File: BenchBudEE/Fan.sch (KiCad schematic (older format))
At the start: 0 parts

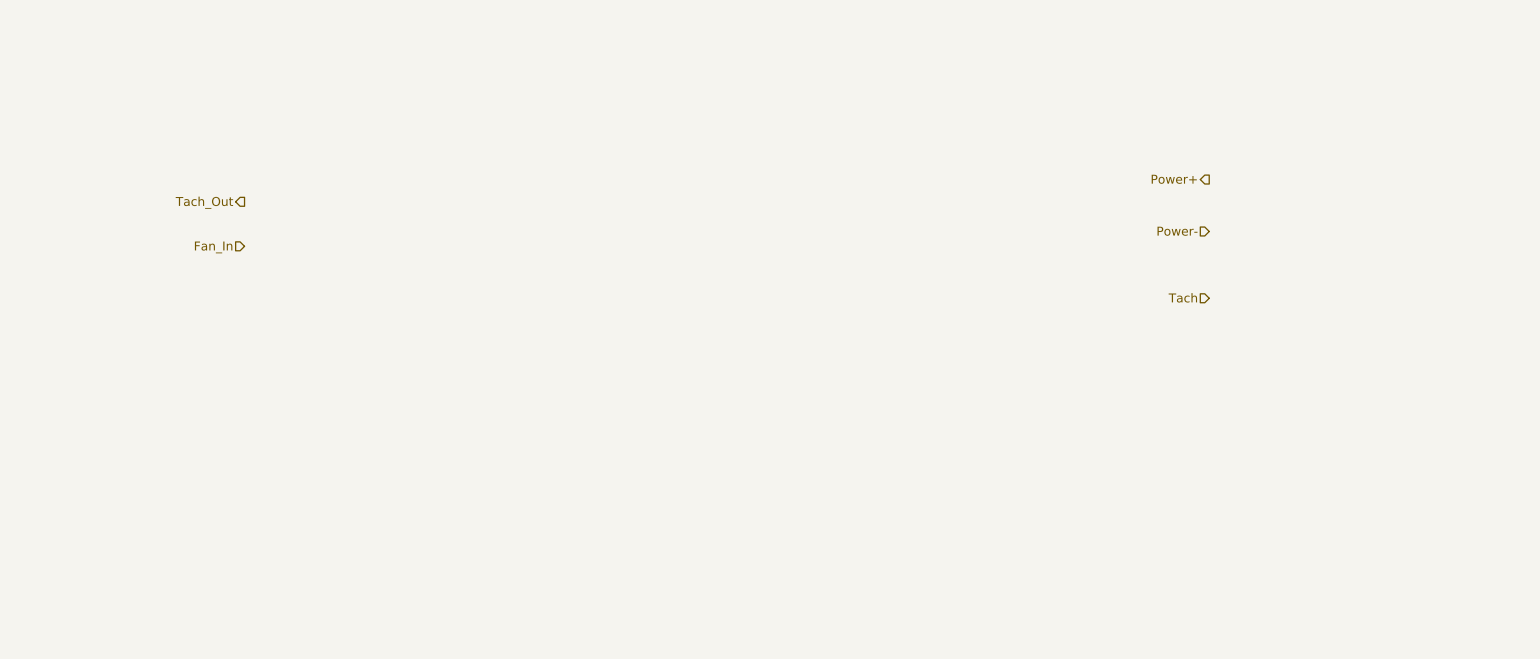
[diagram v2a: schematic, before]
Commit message: Roughly filled in the Fan sheet.
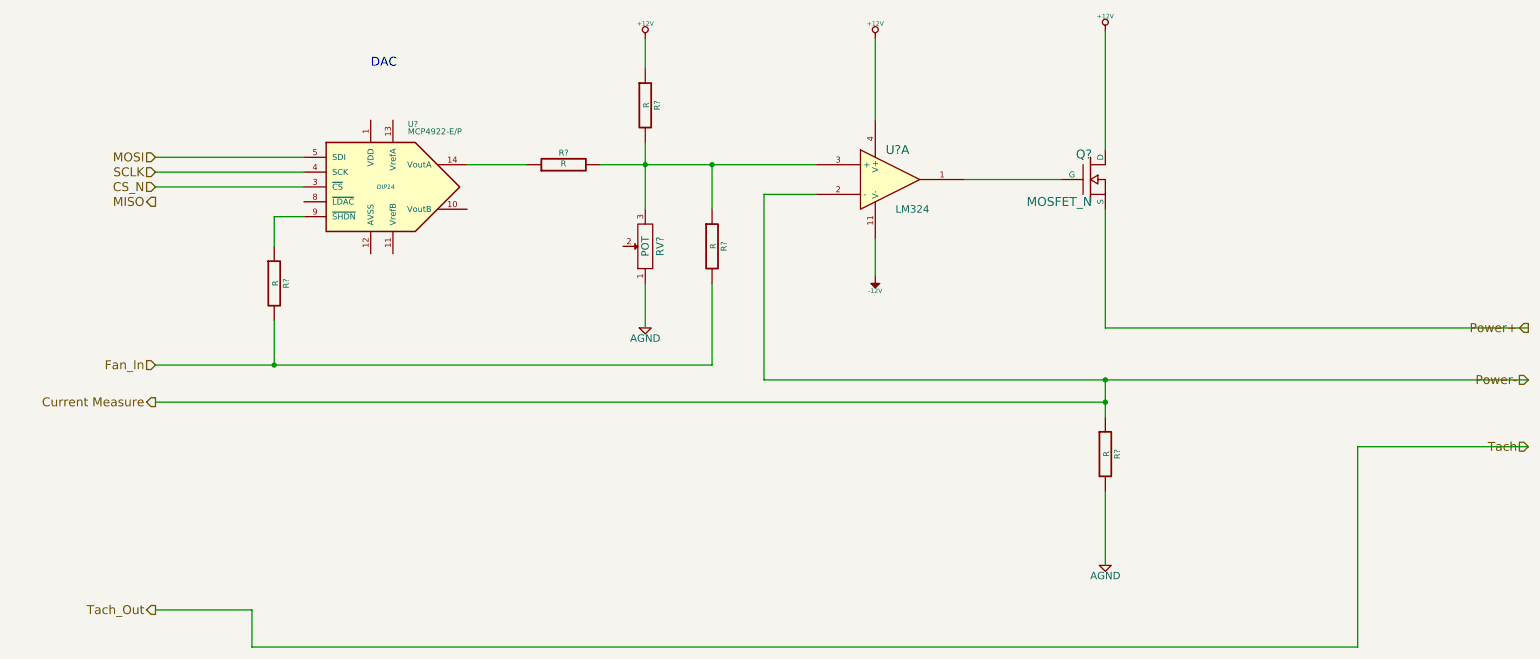
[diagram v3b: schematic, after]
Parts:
- added Q?: MOSFET_N, ~, symbol MOSFET_N
- added R? (x5): R, ~, symbol R
- added RV?: POT, ~, symbol POT
- added U?: LM324, symbol LM324
- added U?: MCP4922-E/P, DIP14, symbol MCP4922-E/P
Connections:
- net Fan_In: now also R?.2, R?.2
- net Power+: now also Q?.S
- new net: Q?.G, U?.1
- new net: R?.1, R?.2, R?.2, RV?.3, U?.3 (+)
- new net: R?.1, U?.14 (VoutA)
- new net: R?.1, U?.9 (~SHDN~)
- new net +12V: Q?.D, R?.1, U?.4 (V+)
- new net -12V: U?.11 (V-)
- new net AGND: R?.2, RV?.1
- new net CS_N: U?.3 (~CS~)
- new net Current Measure: R?.1, U?.2 (-)
- new net MOSI: U?.5 (SDI)
- new net SCLK: U?.4 (SCK)
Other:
- note added: "DAC"

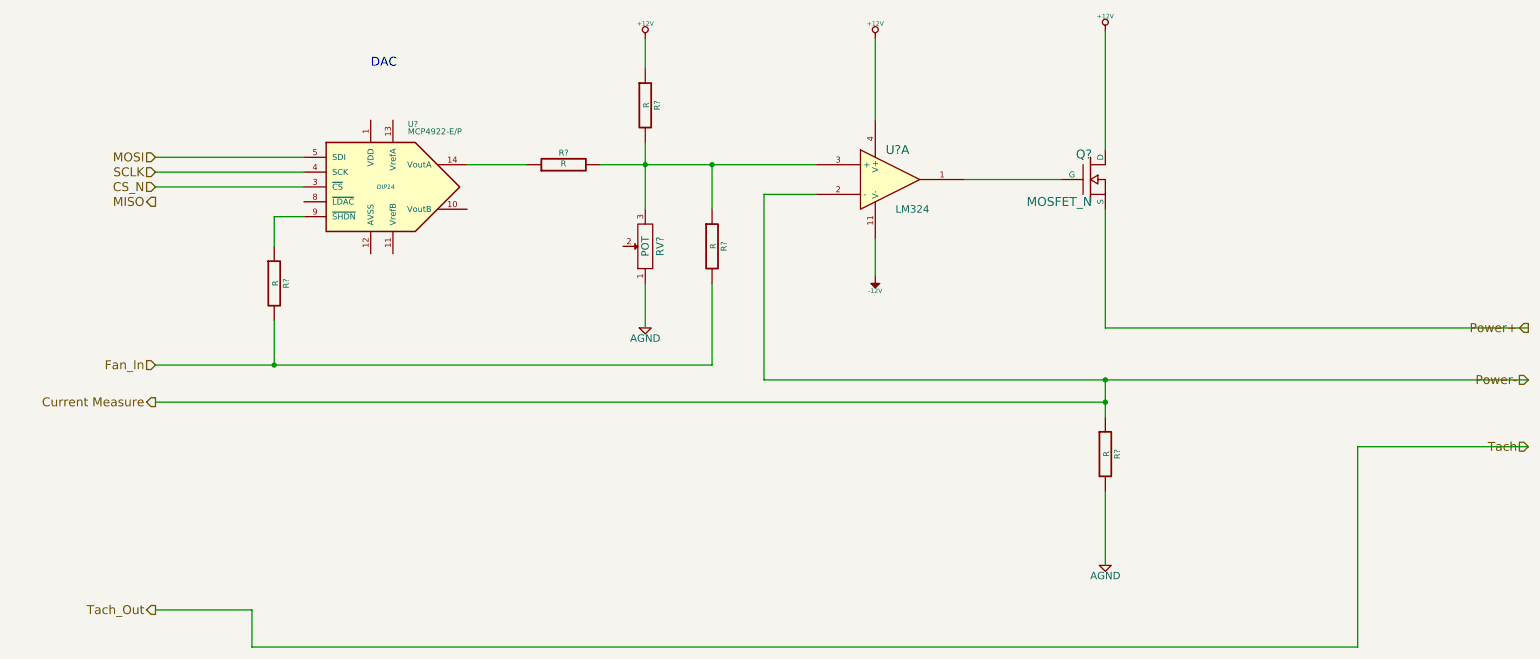
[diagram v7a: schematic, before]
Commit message: Populated the Arduino block and top level wiring.
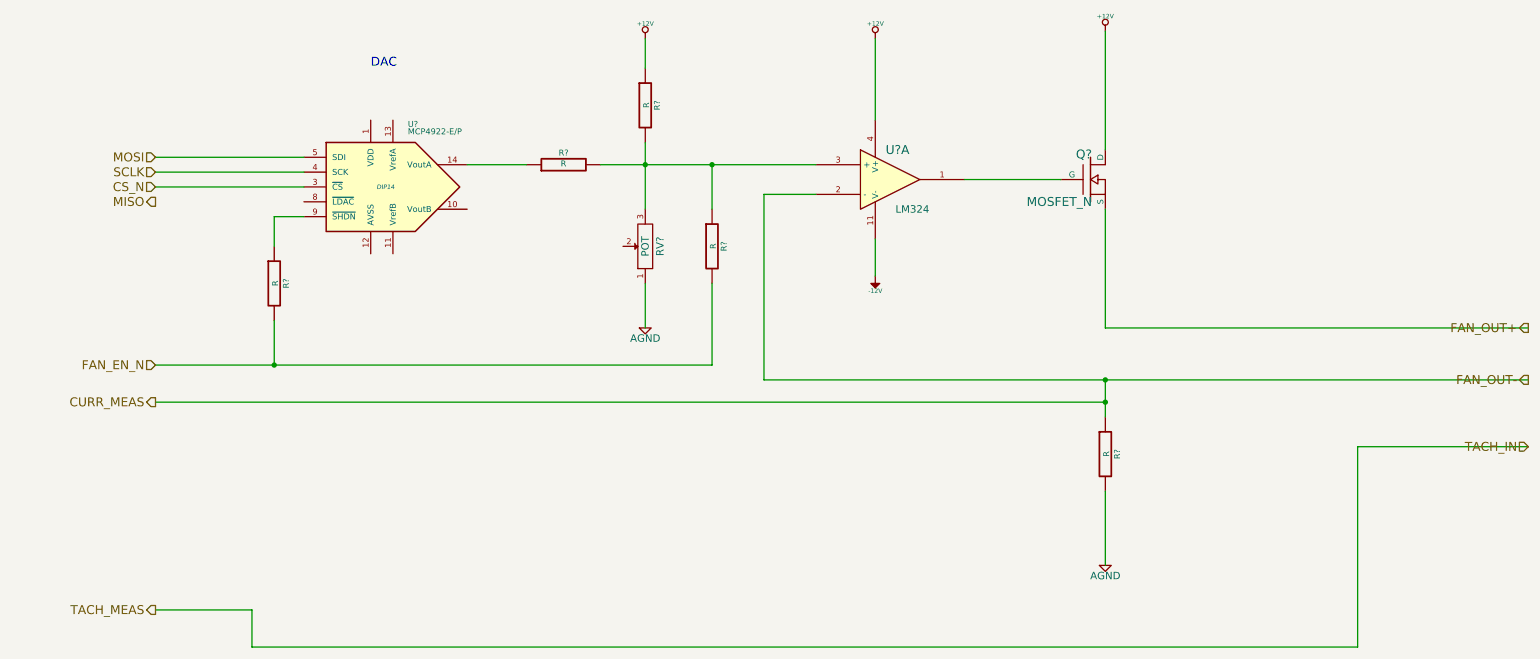
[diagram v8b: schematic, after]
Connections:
- net Current Measure renamed CURR_MEAS
- net Fan_In renamed FAN_EN_N
- net Power+ renamed FAN_OUT+
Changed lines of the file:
@@
 $Descr A4 11693 8268
 encoding utf-8
-Sheet 7 9
+Sheet 9 9
 Title ""
 Date "10 feb 2014"
@@
 $EndDescr
 Text HLabel 10650 3700 0    60   Output ~ 0
-Power+
-Text HLabel 10650 4050 0    60   Input ~ 0
-Power-
+FAN_OUT+
+Text HLabel 10650 4050 0    60   Output ~ 0
+FAN_OUT-
 Text HLabel 10650 4500 0    60   Input ~ 0
-Tach
+TACH_IN
 Text HLabel 1400 5600 0    60   Output ~ 0
-Tach_Out
+TACH_MEAS
 Text HLabel 1400 3950 0    60   Input ~ 0
-Fan_In
+FAN_EN_N
 $Comp
 L LM324 U?
@@
 	9500 5850 2050 5850
 Text HLabel 1400 4200 0    60   Output ~ 0
-Current Measure
+CURR_MEAS
 Wire Wire Line
 	2050 5850 2050 5600
